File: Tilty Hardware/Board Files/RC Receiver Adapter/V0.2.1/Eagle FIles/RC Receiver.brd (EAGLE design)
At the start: 38.1 x 50.8 mm, 32 parts, among them U1 ATMEGA328P, U2 LM2931, U3 AP7313SOT23R, U4 PCA9306, Y1 16MHz

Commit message: Minor tweaks and changes
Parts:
- moved C6 0.51 mm to (8.76, 6.99)
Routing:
- net GND: track 195.5 -> 184.3 mm
- net +5V: track 169.5 -> 167.2 mm
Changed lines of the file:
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@@
 <text x="34.544" y="15.494" size="1.778" layer="26" ratio="12" rot="MR0">ASDA</text>
 <text x="34.544" y="12.954" size="1.778" layer="26" ratio="12" rot="MR0">ASCL</text>
+<text x="33.401" y="48.26" size="1.27" layer="25" ratio="15" rot="R90">5v</text>
+<text x="5.334" y="46.482" size="1.27" layer="25" ratio="15" rot="R75">3v3</text>
+<text x="35.306" y="9.906" size="1.27" layer="25" ratio="15" rot="R240">GND</text>
 </plain>
 <attributes>
@@
 <element name="JP3" library="My Parts" package="8-PIN_RECEPTACLE_LOCK_NO-SS" value="8-PIN_HEADER" x="35.56" y="20.193" rot="R90"/>
 <element name="JP4" library="My Parts" package="8-PIN_RECEPTACLE_LOCK_NO-SS" value="8-PIN_HEADER" x="30.48" y="40.513" rot="R90"/>
-<element name="C6" library="resistor" package="C0603" value="4.7uF" x="9.271" y="6.985" smashed="yes" rot="R180"/>
+<element name="C6" library="resistor" package="C0603" value="4.7uF" x="8.763" y="6.985" smashed="yes" rot="R180"/>
 <element name="C7" library="resistor" package="C0603" value="0.1uF" x="5.2705" y="6.985" smashed="yes"/>
 <element name="SJ1" library="SparkFun-Passives" package="SJ_2S-TRACE" value="SOLDERJUMPERTRACE" x="2.54" y="8.636" smashed="yes"/>
@@
 <wire x1="8.167" y1="9.0315" x2="6.1205" y2="6.985" width="0.508" layer="1"/>
 <wire x1="8.167" y1="9.0315" x2="8.167" y2="7.239" width="0.508" layer="1"/>
-<wire x1="8.167" y1="7.239" x2="8.421" y2="6.985" width="0.508" layer="1"/>
-<wire x1="8.382" y1="6.946" x2="8.421" y2="6.985" width="0.508" layer="1"/>
+<wire x1="8.167" y1="7.239" x2="7.913" y2="6.985" width="0.508" layer="1"/>
+<wire x1="8.128" y1="6.946" x2="7.913" y2="6.985" width="0.508" layer="1"/>
 <wire x1="20.25" y1="30.677" x2="20.25" y2="42.234" width="0.254" layer="1"/>
 <wire x1="20.25" y1="42.234" x2="19.304" y2="43.18" width="0.254" layer="1"/>
@@
 <wire x1="19.431" y1="22.479" x2="19.431" y2="21.1264" width="0.1524" layer="1"/>
 <wire x1="19.431" y1="21.1264" x2="19.45" y2="21.1074" width="0.1524" layer="1"/>
-<wire x1="25.781" y1="1.778" x2="27.432" y2="1.778" width="0.3048" layer="1"/>
-<wire x1="27.432" y1="1.778" x2="29.464" y2="3.81" width="0.3048" layer="1"/>
-<wire x1="29.464" y1="3.81" x2="29.464" y2="5.08" width="0.3048" layer="1"/>
-<wire x1="29.464" y1="5.08" x2="30.48" y2="6.096" width="0.3048" layer="1"/>
-<wire x1="30.48" y1="6.096" x2="33.782" y2="6.096" width="0.3048" layer="1"/>
-<wire x1="33.782" y1="6.096" x2="34.544" y2="6.858" width="0.3048" layer="1"/>
 <wire x1="35.687" y1="11.303" x2="34.4805" y2="10.2235" width="0.3048" layer="16"/>
 <wire x1="34.4805" y1="10.2235" x2="34.4805" y2="6.7945" width="0.3048" layer="16"/>
@@
 <wire x1="20.2565" y1="28.2575" x2="20.2565" y2="29.6861" width="0.2032" layer="1"/>
 <wire x1="20.2565" y1="29.6861" x2="20.25" y2="29.6926" width="0.2032" layer="1"/>
-<wire x1="8.382" y1="6.946" x2="8.382" y2="3.048" width="0.508" layer="1"/>
-<wire x1="8.382" y1="3.048" x2="9.652" y2="1.778" width="0.508" layer="1"/>
-<wire x1="9.652" y1="1.778" x2="11.811" y2="1.778" width="0.508" layer="1"/>
+<wire x1="8.128" y1="6.946" x2="8.128" y2="3.048" width="0.508" layer="1"/>
+<wire x1="8.128" y1="3.048" x2="9.398" y2="1.778" width="0.508" layer="1"/>
+<wire x1="9.398" y1="1.778" x2="11.811" y2="1.778" width="0.508" layer="1"/>
 <wire x1="29.552" y1="15.367" x2="29.552" y2="17.78" width="0.2032" layer="1"/>
 <wire x1="29.552" y1="15.367" x2="32.986" y2="15.367" width="0.2032" layer="1"/>
@@
 <wire x1="20.574" y1="46.863" x2="23.749" y2="46.863" width="0.3175" layer="16"/>
 <wire x1="23.749" y1="46.863" x2="26.289" y2="46.863" width="0.3175" layer="16"/>
-<wire x1="15.494" y1="21.844" x2="16.002" y2="22.352" width="0.254" layer="1"/>
-<wire x1="16.002" y1="22.352" x2="16.764" y2="22.352" width="0.254" layer="1"/>
-<wire x1="16.764" y1="22.352" x2="17.018" y2="22.098" width="0.254" layer="1"/>
-<wire x1="17.018" y1="22.098" x2="17.018" y2="21.1394" width="0.254" layer="1"/>
 <wire x1="17.018" y1="21.1394" x2="17.05" y2="21.1074" width="0.254" layer="1"/>
 <wire x1="17.05" y1="21.1074" x2="17.05" y2="19.692" width="0.381" layer="1"/>
@@
 <wire x1="10.8458" y1="10.8458" x2="11.684" y2="11.684" width="0.508" layer="1"/>
 <wire x1="11.684" y1="11.684" x2="11.684" y2="18.796" width="0.508" layer="1"/>
-<wire x1="16.764" y1="22.352" x2="16.764" y2="25.654" width="0.2032" layer="1"/>
-<wire x1="16.764" y1="25.654" x2="17.018" y2="25.908" width="0.2032" layer="1"/>
-<wire x1="17.85" y1="29.6926" x2="17.85" y2="28.378" width="0.2032" layer="1"/>
-<wire x1="17.85" y1="28.378" x2="18.288" y2="27.94" width="0.2032" layer="1"/>
-<wire x1="18.288" y1="27.94" x2="18.288" y2="26.416" width="0.2032" layer="1"/>
-<wire x1="18.288" y1="26.416" x2="17.78" y2="25.908" width="0.2032" layer="1"/>
-<wire x1="17.78" y1="25.908" x2="17.018" y2="25.908" width="0.2032" layer="1"/>
+<wire x1="17.018" y1="21.1394" x2="17.018" y2="25.146" width="0.2032" layer="1"/>
 <wire x1="37.338" y1="33.782" x2="37.338" y2="21.844" width="0.508" layer="1"/>
 <wire x1="37.338" y1="21.844" x2="37.338" y2="10.922" width="0.508" layer="1"/>
@@
 <wire x1="31.369" y1="49.403" x2="32.512" y2="48.26" width="0.508" layer="1"/>
 <wire x1="9.906" y1="9.5758" x2="9.906" y2="7.2" width="0.508" layer="1"/>
-<wire x1="9.906" y1="7.2" x2="10.121" y2="6.985" width="0.508" layer="1"/>
-<wire x1="11.811" y1="4.318" x2="10.922" y2="4.318" width="0.508" layer="1"/>
-<wire x1="10.922" y1="4.318" x2="10.16" y2="5.08" width="0.508" layer="1"/>
-<wire x1="10.16" y1="5.08" x2="10.16" y2="6.946" width="0.508" layer="1"/>
-<wire x1="10.16" y1="6.946" x2="10.121" y2="6.985" width="0.508" layer="1"/>
-<wire x1="15.494" y1="21.844" x2="14.732" y2="21.844" width="0.254" layer="1"/>
+<wire x1="9.906" y1="7.2" x2="9.613" y2="6.985" width="0.508" layer="1"/>
+<wire x1="11.811" y1="4.318" x2="10.668" y2="4.318" width="0.508" layer="1"/>
+<wire x1="10.668" y1="4.318" x2="9.906" y2="5.08" width="0.508" layer="1"/>
+<wire x1="9.906" y1="5.08" x2="9.906" y2="6.946" width="0.508" layer="1"/>
+<wire x1="9.906" y1="6.946" x2="9.613" y2="6.985" width="0.508" layer="1"/>
 <wire x1="6.096" y1="22.098" x2="6.096" y2="23.788" width="0.254" layer="1"/>
 <contactref element="R5" pad="2"/>
@@
 <wire x1="28.956" y1="23.368" x2="28.211" y2="23.368" width="0.2032" layer="1"/>
 <wire x1="28.211" y1="23.368" x2="28.084" y2="23.241" width="0.2032" layer="1"/>
-<wire x1="19.45" y1="29.6926" x2="19.45" y2="28.34" width="0.2032" layer="1"/>
-<wire x1="19.45" y1="28.34" x2="19.05" y2="27.94" width="0.2032" layer="1"/>
-<wire x1="19.05" y1="27.94" x2="18.288" y2="27.94" width="0.2032" layer="1"/>
 <wire x1="36.5055" y1="34.6145" x2="37.338" y2="33.782" width="0.508" layer="1"/>
 <wire x1="33.528" y1="34.6145" x2="36.5055" y2="34.6145" width="0.508" layer="1"/>
@@
 <wire x1="11.684" y1="20.32" x2="12.192" y2="19.812" width="0.254" layer="1"/>
 <wire x1="12.192" y1="19.812" x2="12.192" y2="19.304" width="0.254" layer="1"/>
+<wire x1="17.018" y1="25.146" x2="17.526" y2="25.654" width="0.2032" layer="1"/>
+<wire x1="17.526" y1="25.654" x2="17.907" y2="25.654" width="0.2032" layer="1"/>
+<wire x1="17.907" y1="25.654" x2="18.669" y2="26.416" width="0.2032" layer="1"/>
+<wire x1="18.669" y1="26.416" x2="18.669" y2="27.813" width="0.2032" layer="1"/>
+<wire x1="18.669" y1="27.813" x2="17.8435" y2="28.6385" width="0.2032" layer="1"/>
+<wire x1="17.8435" y1="28.6385" x2="17.8435" y2="29.6861" width="0.2032" layer="1"/>
+<wire x1="17.8435" y1="29.6861" x2="17.85" y2="29.6926" width="0.2032" layer="1"/>
+<wire x1="19.45" y1="29.6926" x2="19.45" y2="28.594" width="0.2032" layer="1"/>
+<wire x1="19.45" y1="28.594" x2="18.669" y2="27.813" width="0.2032" layer="1"/>
 </signal>
 <signal name="N$5">

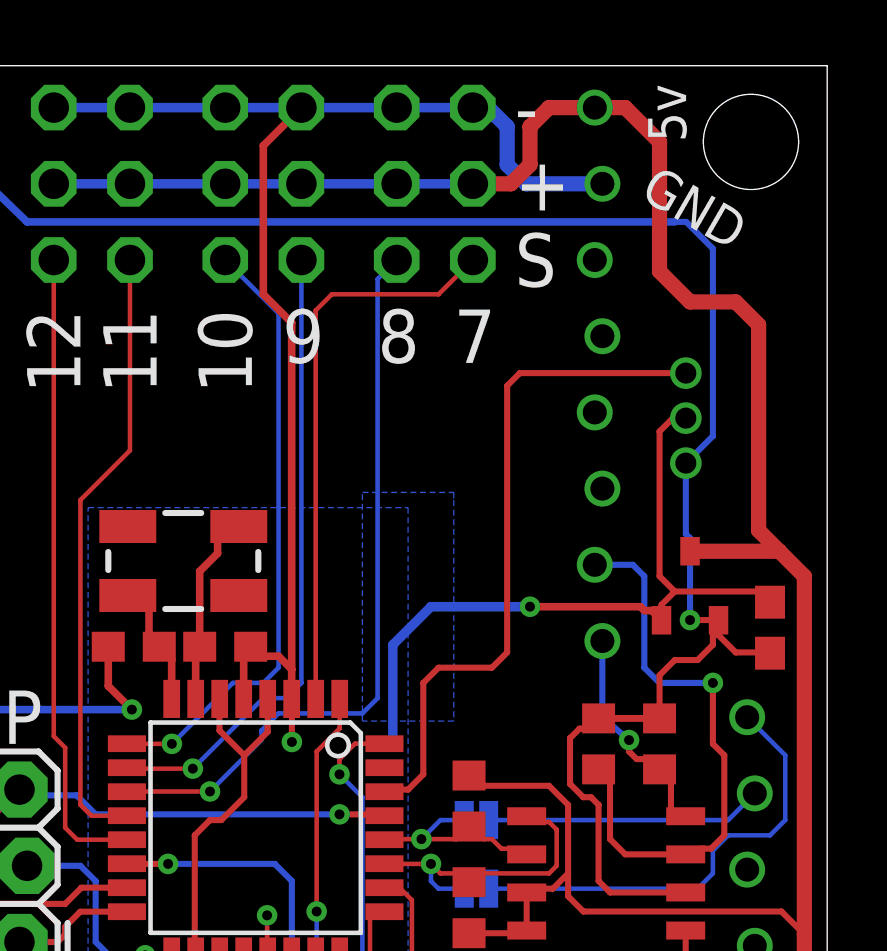
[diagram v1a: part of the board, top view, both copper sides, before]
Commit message: Added serial breakout to R/C adapter
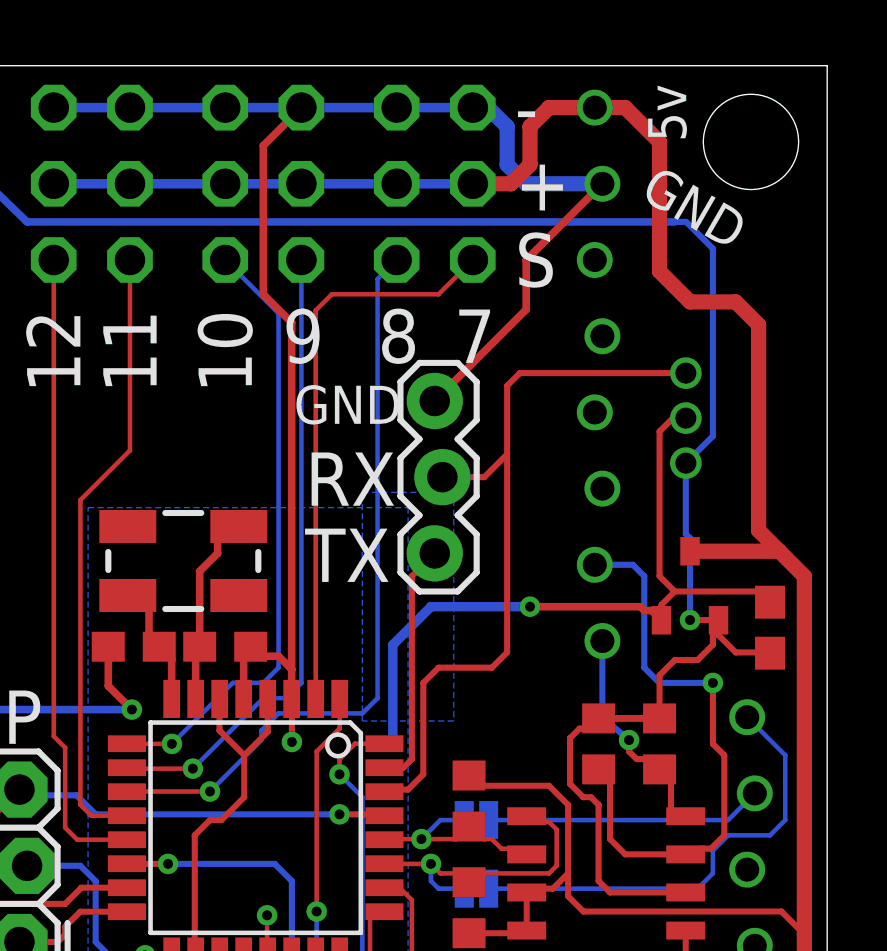
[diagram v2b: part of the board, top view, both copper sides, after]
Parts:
- added JP9: (no value), SparkFun-Connectors:1X03_LOCK
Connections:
- net GND: now also JP9.3
- net RX: now also JP9.2
- net TX: now also JP9.1
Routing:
- net GND: track 184.3 -> 193.8 mm
- net TX: track 0.00 -> 8.21 mm
- net RX: track 22.8 -> 25.3 mm
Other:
- board text added: "RX"
- board text added: "TX"
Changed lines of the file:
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@@
 <rectangle x1="14.07969375" y1="33.84455625" x2="14.1000125" y2="33.864875" layer="26" rot="R213.3"/>
 <text x="19.74198125" y="29.20243125" size="1.905" layer="26" font="vector" ratio="17" rot="MR1.7">IMU</text>
-<text x="19.05" y="38.1" size="1.778" layer="26" ratio="12" rot="MR0" align="center">R/C Receiver</text>
-<text x="19.05" y="36.068" size="1.778" layer="26" ratio="12" rot="MR0" align="center">Add-on</text>
+<text x="19.304" y="19.558" size="1.778" layer="26" ratio="12" rot="MR0" align="center">R/C Receiver</text>
+<text x="19.05" y="17.272" size="1.778" layer="26" ratio="12" rot="MR0" align="center">Add-on</text>
 <text x="7.0485" y="28.194" size="1.778" layer="25" ratio="12">ICSP</text>
 <text x="26.924" y="12.192" size="1.778" layer="25" ratio="15">PWR</text>
 <text x="0.635" y="34.544" size="1.27" layer="25" ratio="15">Reset</text>
-<text x="29.21" y="48.768" size="1.27" layer="26" ratio="15" rot="MR0">5v</text>
+<text x="29.464" y="48.768" size="1.27" layer="26" ratio="15" rot="MR0">5v</text>
 <text x="34.036" y="44.196" size="1.27" layer="26" ratio="15" rot="MR30">GND</text>
-<text x="11.938" y="48.768" size="1.27" layer="26" ratio="15" rot="MR0">3v3</text>
+<text x="11.176" y="47.244" size="1.27" layer="26" ratio="15" rot="MR32.5">3v3</text>
 <text x="35.56" y="45.72" size="1.27" layer="25" ratio="15" rot="R150">GND</text>
 <text x="8.382" y="45.974" size="1.778" layer="26" ratio="12" rot="MR0" align="bottom-right">0</text>
@@
 <text x="29.464" y="30.734" size="1.778" layer="26" ratio="12" rot="MR0">18</text>
 <text x="29.464" y="33.274" size="1.778" layer="26" ratio="12" rot="MR0">19</text>
-<text x="29.464" y="35.814" size="1.27" layer="26" ratio="15" rot="MR0">20</text>
-<text x="29.464" y="39.116" size="1.27" layer="26" ratio="15" rot="MR0">21</text>
+<text x="29.464" y="35.814" size="1.778" layer="26" ratio="12" rot="MR0">20</text>
+<text x="29.464" y="38.354" size="1.778" layer="26" ratio="12" rot="MR0">21</text>
 <text x="29.464" y="40.894" size="1.778" layer="26" ratio="12" rot="MR0">22</text>
 <text x="34.544" y="10.414" size="1.778" layer="26" ratio="12" rot="MR0">GND</text>
-<text x="29.464" y="43.434" size="1.778" layer="26" ratio="12" rot="MR0">23</text>
+<text x="29.464" y="43.688" size="1.27" layer="26" ratio="15" rot="MR0">23</text>
 <text x="34.544" y="15.494" size="1.778" layer="26" ratio="12" rot="MR0">ASDA</text>
 <text x="34.544" y="12.954" size="1.778" layer="26" ratio="12" rot="MR0">ASCL</text>
@@
 <text x="5.334" y="46.482" size="1.27" layer="25" ratio="15" rot="R75">3v3</text>
 <text x="35.306" y="9.906" size="1.27" layer="25" ratio="15" rot="R240">GND</text>
+<text x="20.701" y="36.1315" size="1.778" layer="25" ratio="12">RX</text>
+<text x="20.701" y="33.5915" size="1.778" layer="25" ratio="12">TX</text>
+<text x="20.32" y="38.862" size="1.27" layer="25" ratio="15">GND</text>
 </plain>
 <attributes>
@@
 <element name="SJ2" library="SparkFun-Passives" package="SJ_2S-NOTRACE" value="SOLDERJUMPERNC2" x="26.416" y="25.654" smashed="yes" rot="MR0"/>
 <element name="SJ3" library="SparkFun-Passives" package="SJ_2S-NOTRACE" value="SOLDERJUMPERNC2" x="26.416" y="23.368" smashed="yes" rot="MR0"/>
+<element name="JP9" library="SparkFun-Connectors" package="1X03_LOCK" value="" x="25.146" y="34.544" smashed="yes" rot="R90">
+<attribute name="VALUE" x="28.321" y="33.274" size="1.27" layer="27" rot="R90"/>
+</element>
 </elements>
 <signals>
@@
 <wire x1="23.622" y1="14.224" x2="23.622" y2="15.748" width="0.508" layer="1"/>
 <wire x1="7.62" y1="16.764" x2="7.62" y2="17.78" width="0.508" layer="1"/>
+<contactref element="JP9" pad="3"/>
+<wire x1="25.019" y1="39.624" x2="28.067" y2="42.672" width="0.254" layer="1"/>
+<wire x1="28.067" y1="42.672" x2="28.067" y2="44.323" width="0.254" layer="1"/>
+<wire x1="28.067" y1="44.323" x2="30.607" y2="46.863" width="0.254" layer="1"/>
 </signal>
 <signal name="+24V">
@@
 <wire x1="33.3885" y1="40.5525" x2="27.8525" y2="40.5525" width="0.2032" layer="1"/>
 <wire x1="27.8525" y1="40.5525" x2="27.432" y2="40.132" width="0.2032" layer="1"/>
-<wire x1="27.432" y1="40.132" x2="27.432" y2="31.242" width="0.2032" layer="1"/>
+<wire x1="27.432" y1="37.846" x2="27.432" y2="31.242" width="0.2032" layer="1"/>
 <wire x1="27.432" y1="31.242" x2="26.924" y2="30.734" width="0.2032" layer="1"/>
 <wire x1="26.924" y1="30.734" x2="25.146" y2="30.734" width="0.2032" layer="1"/>
@@
 <wire x1="24.13" y1="26.67" x2="23.4126" y2="26.67" width="0.2032" layer="1"/>
 <wire x1="23.4126" y1="26.67" x2="23.3426" y2="26.6" width="0.2032" layer="1"/>
+<contactref element="JP9" pad="2"/>
+<wire x1="27.432" y1="40.132" x2="27.432" y2="37.846" width="0.2032" layer="1"/>
+<wire x1="27.432" y1="37.846" x2="26.67" y2="37.084" width="0.2032" layer="1"/>
+<wire x1="26.67" y1="37.084" x2="25.273" y2="37.084" width="0.2032" layer="1"/>
 </signal>
 <signal name="+3V3">
@@
 <signal name="TX">
 <contactref element="U1" pad="31"/>
+<contactref element="JP9" pad="1"/>
+<wire x1="23.3426" y1="27.4" x2="23.971" y2="27.4" width="0.2032" layer="1"/>
+<wire x1="23.971" y1="27.4" x2="24.257" y2="27.686" width="0.2032" layer="1"/>
+<wire x1="24.257" y1="27.686" x2="24.257" y2="33.782" width="0.2032" layer="1"/>
+<wire x1="24.257" y1="33.782" x2="25.019" y2="34.544" width="0.2032" layer="1"/>
 </signal>
 <signal name="STATUS_LED">
